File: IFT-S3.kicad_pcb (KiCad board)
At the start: 2 copper layers, 54 x 85.6 mm, 38 parts, among them J1 Conn_01x04_Socket, J2 Conn_01x01_Pin, J3 Conn_01x02_Pin, J6 Conn_01x02_Pin, J7 Conn_01x02, Q1 Q_Photo_NPN, Q2 Q_NMOS_GSD, Q3 IRFZ44N, SW2 PTS526_SK15_SMTR2_LFS, SW3 PTS526_SK15_SMTR2_LFS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

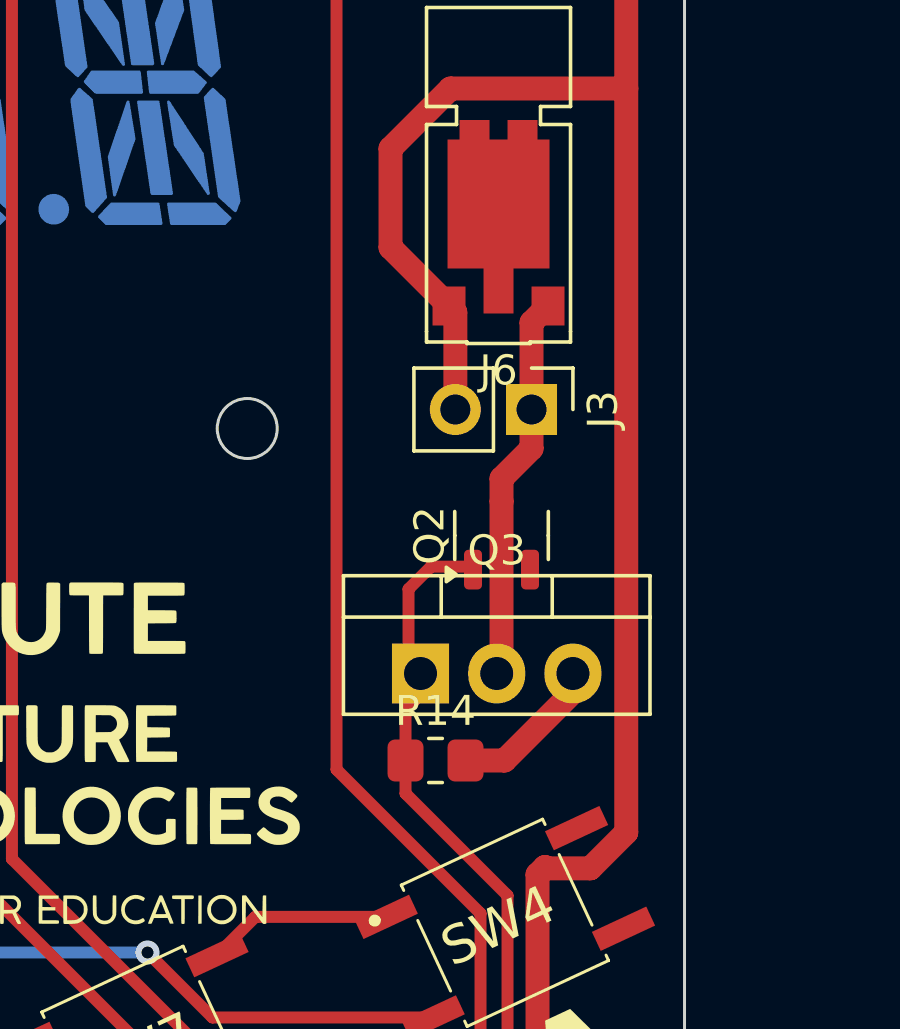
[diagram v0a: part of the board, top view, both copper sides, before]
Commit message: Clean up and OLED 3D model added
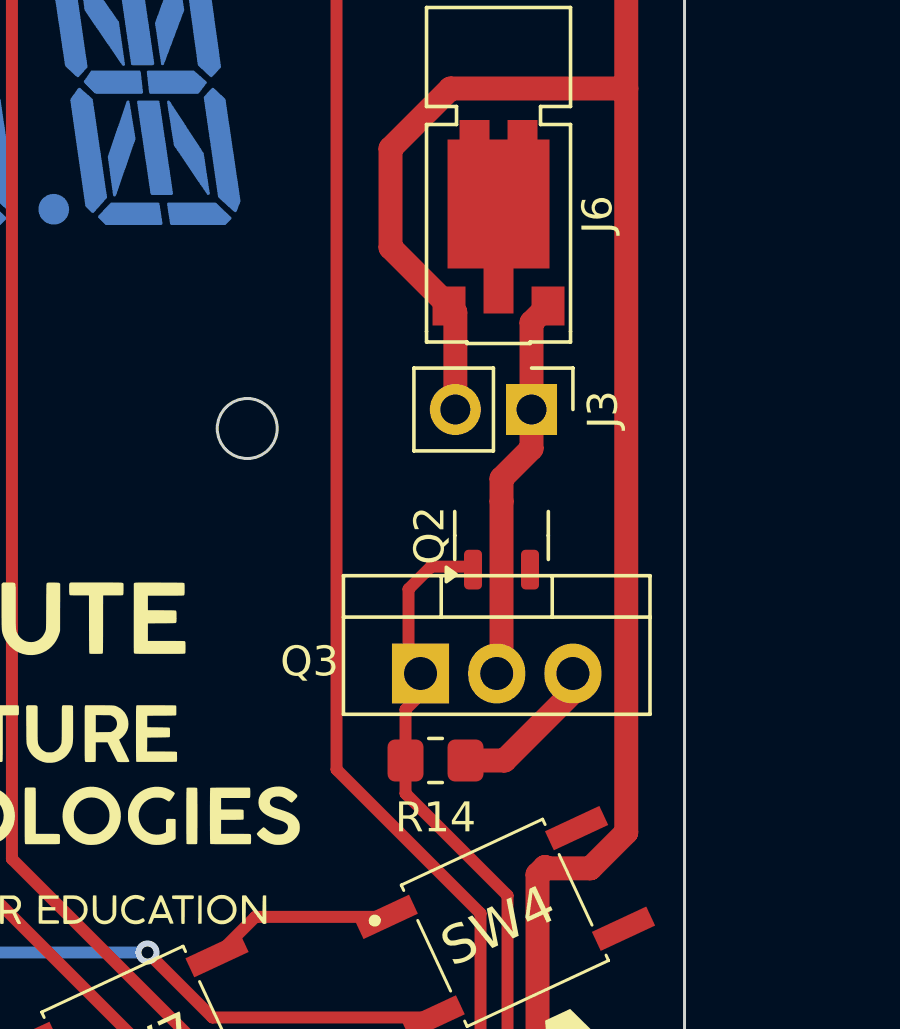
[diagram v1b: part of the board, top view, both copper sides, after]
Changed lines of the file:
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@@
 		)
 		(embedded_fonts no)
+		(model "${KIPRJMOD}/packages3D/DM-OLED096-636--3DModel-STEP-56544.STEP"
+			(offset
+				(xyz 0 -5 0)
+			)
+			(scale
+				(xyz 1.03 1 1.06)
+			)
+			(rotate
+				(xyz -90 -0 -0)
+			)
+		)
 	)
 	(footprint "footprints:PTS526SK15SMTR2LFS"
@@
 		(tags "vibration motor Vybronics")
 		(property "Reference" "J6"
-			(at 0 -6.5 180)
+			(at -3.3 -1.3 270)
 			(layer "F.SilkS")
 			(effects
@@
 		(tags "resistor handsolder")
 		(property "Reference" "R14"
-			(at 0 -1.65 0)
+			(at 0 1.9 0)
 			(layer "F.SilkS")
 			(effects
@@
 		(embedded_fonts no)
 		(model "${KIPRJMOD}/packages3D/PinHeader_1x01_P2.54mm_Vertical.step"
+			(hide yes)
 			(offset
 				(xyz 0 0 0)
@@
 		(tags "TO-220-3 Vertical RM 2.54mm")
 		(property "Reference" "Q3"
-			(at 2.54 -4.1 0)
+			(at -3.7 -0.4 0)
 			(layer "F.SilkS")
 			(effects
